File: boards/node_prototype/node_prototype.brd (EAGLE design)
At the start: 85.1 x 46.9 mm, 31 parts, among them T1 2N2222

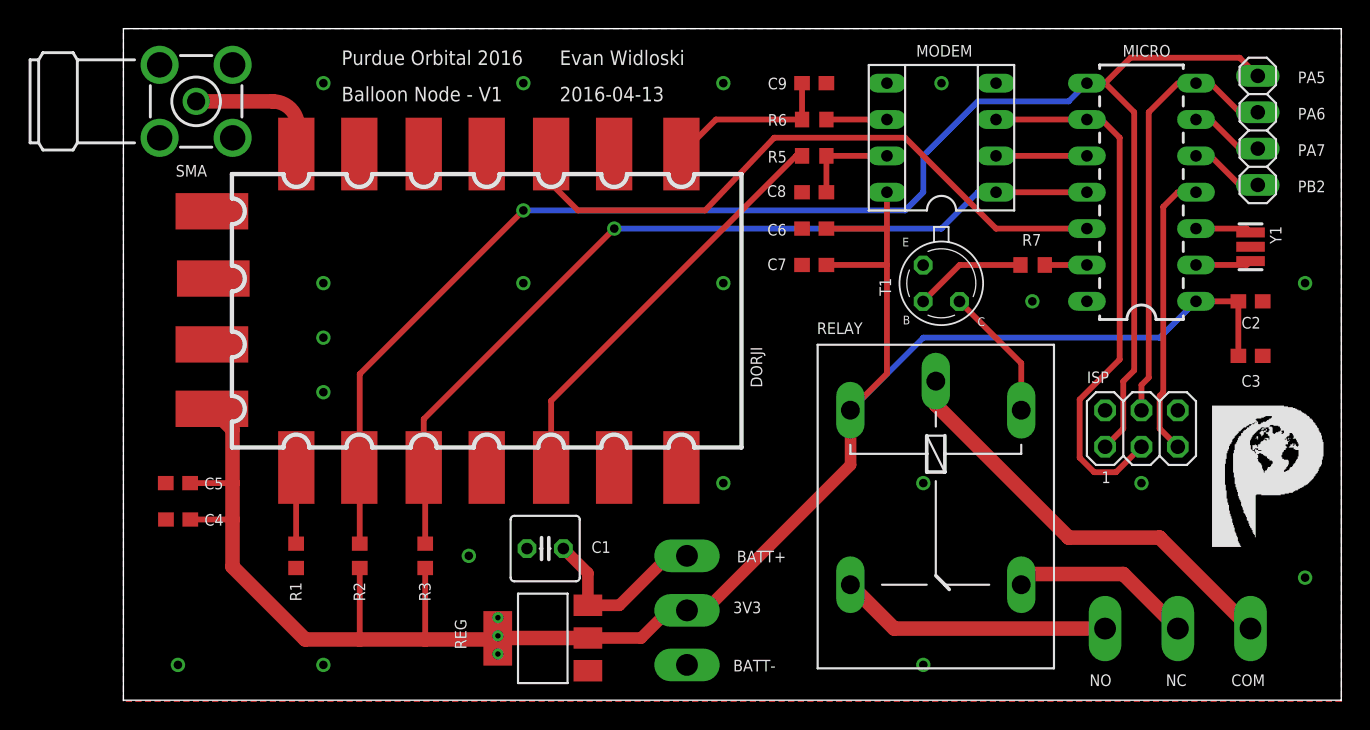
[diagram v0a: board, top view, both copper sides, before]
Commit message: rename rocket radio, add renders
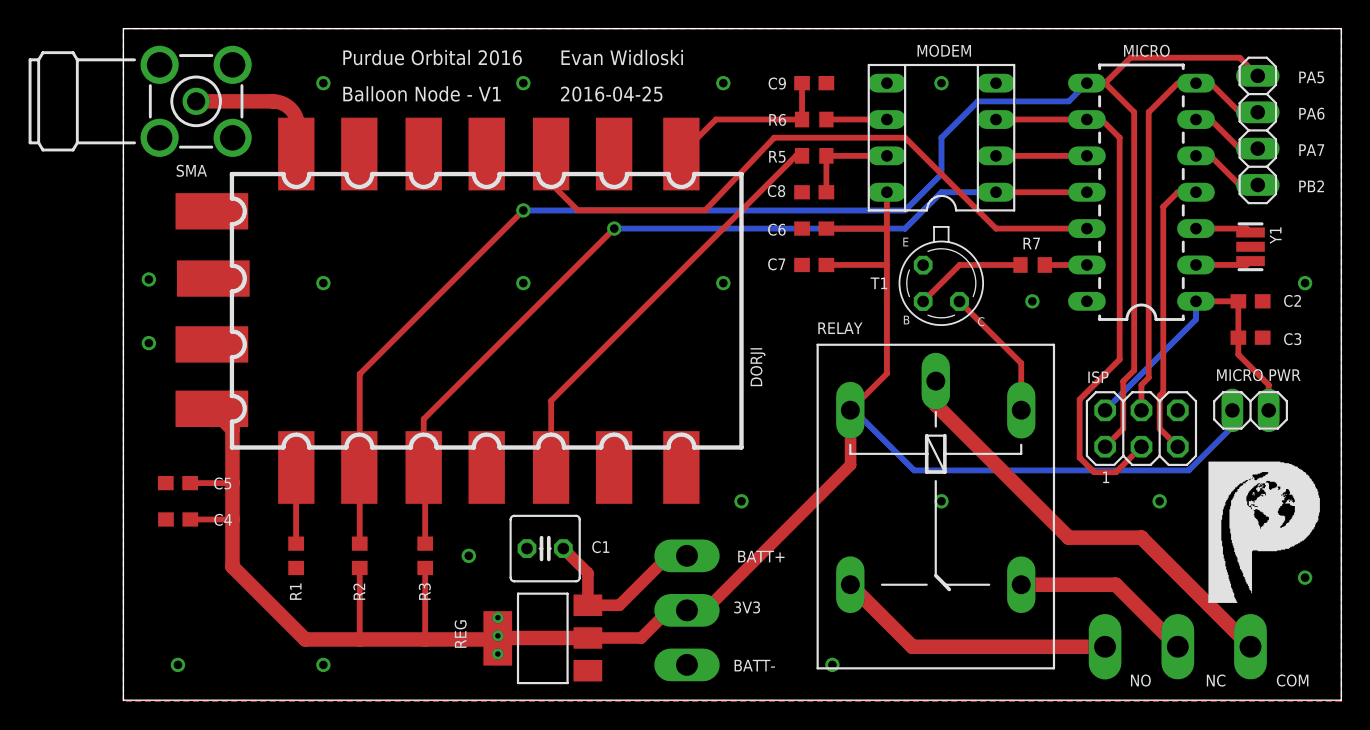
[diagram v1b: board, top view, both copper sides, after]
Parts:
- added JP1: (no value), pinhead:1X02
- moved COM 1.27 mm to (78.7, 3.81)
- moved NC 1.27 mm to (73.7, 3.81)
- moved NO 1.27 mm to (68.6, 3.81)
- moved C3 1.27 mm to (78.7, 25.4)
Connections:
- net +3V3: now also JP1.2; no longer C2.1, C3.1, MICRO.1
- net VCC: now also C2.1, C3.1, JP1.1, MICRO.1
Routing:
- net VCC: track 0.00 -> 21.7 mm
- net +3V3: track 143.4 -> 140.1 mm
- net MOD_SELECT: track 61.6 -> 62.9 mm
- net N$9: track 19.1 -> 19.6 mm
- net N$11: track 30.1 -> 30.6 mm
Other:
- board text added: "2016-04-25"
- board text added: "MICRO PWR"
- board text removed: "2016-04-13"
